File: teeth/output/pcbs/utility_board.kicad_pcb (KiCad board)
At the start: 2 copper layers, 100 x 100 mm, 1 part

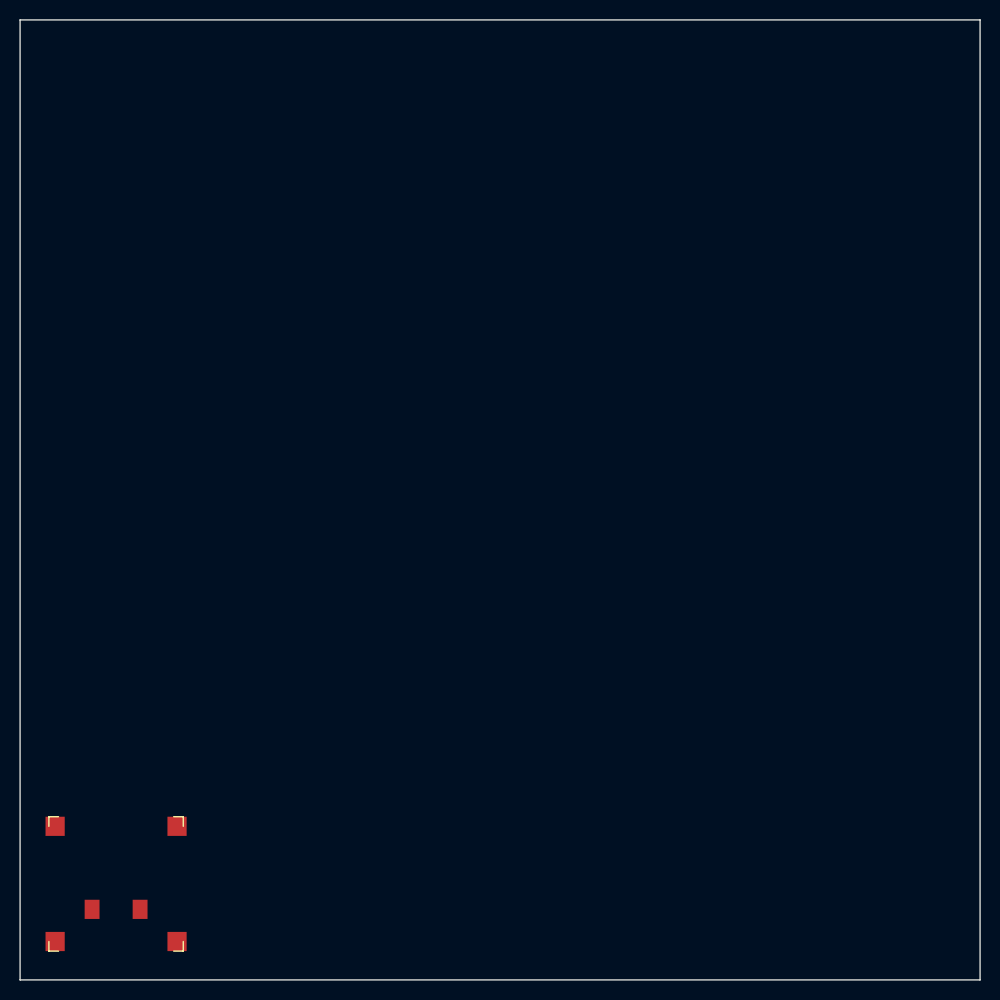
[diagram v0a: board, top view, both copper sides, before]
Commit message: Add xiao cutout footprint to utility board.
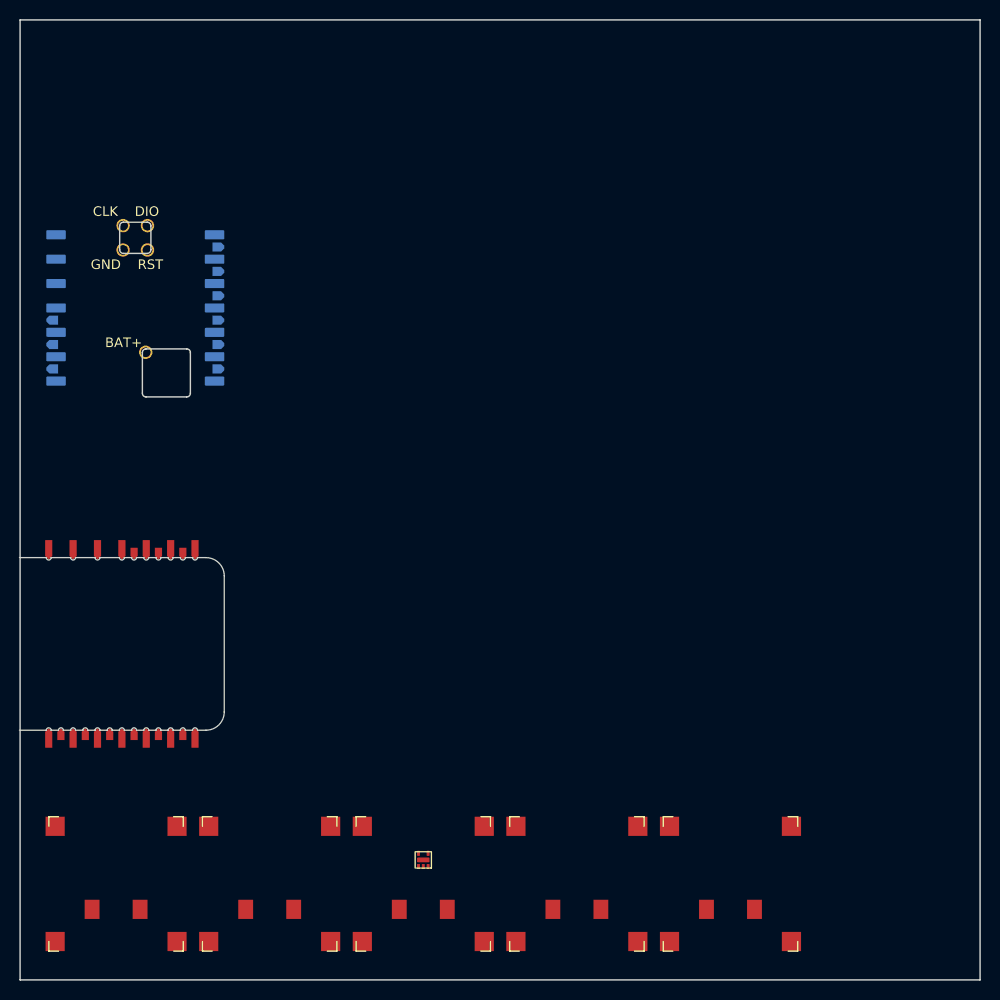
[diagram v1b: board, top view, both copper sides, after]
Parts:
- added D1: , D_MMBD4148PLM, F.Cu at (142.0, 187.5)
- added J1: , xiao_plus_cutout, F.Cu at (110.6, 165.0)
- added S2: , PG1316S, F.Cu at (126.0, 190.0)
- added S3: , PG1316S, F.Cu at (142.0, 190.0)
- added S4: , PG1316S, F.Cu at (158.0, 190.0)
- added S5: , PG1316S, F.Cu at (174.0, 190.0)
- added XX1: , xiao_plus_smd_prod, B.Cu at (112.0, 130.0)
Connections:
- S1 pad 1: firstcol_firstrow -> pinky_home

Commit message: More work on utility board, complex xiao slot complete. Fixed email address.
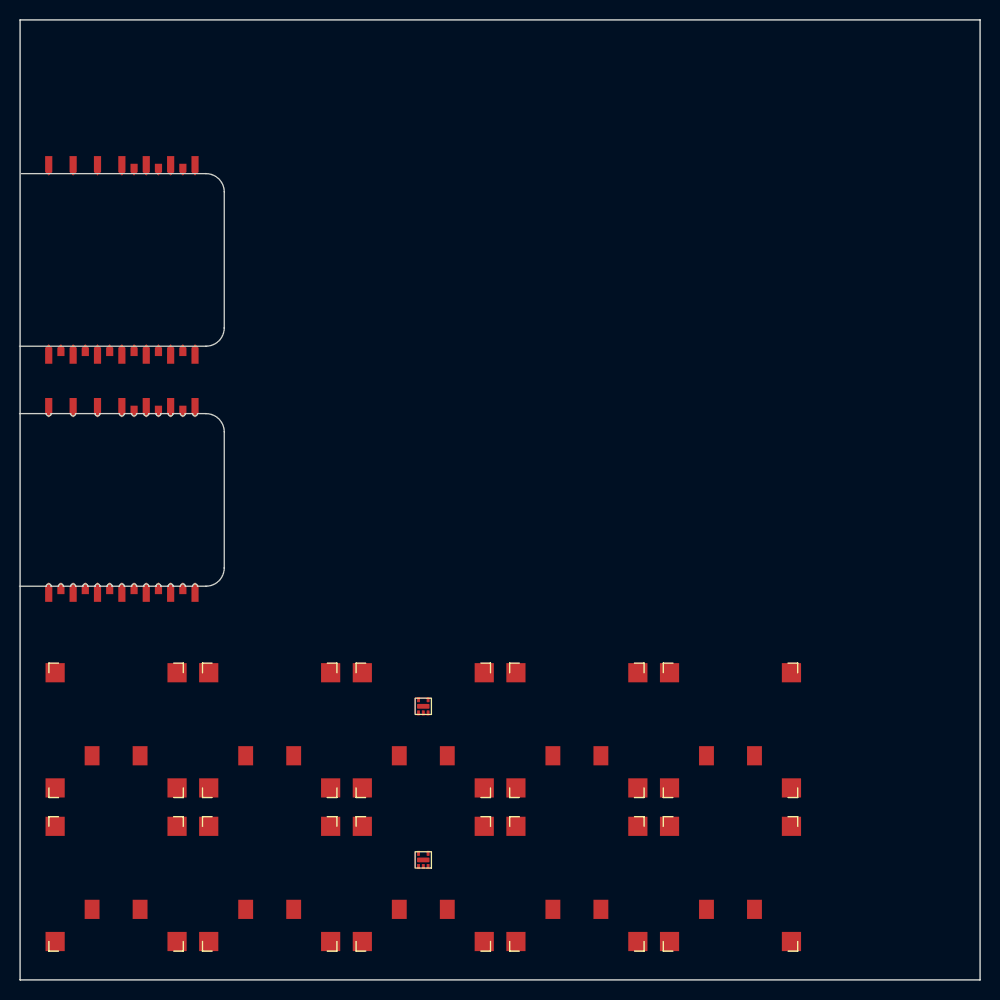
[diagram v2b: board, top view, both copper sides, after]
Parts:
- removed XX1: , xiao_plus_smd_prod
- added D2: , D_MMBD4148PLM, F.Cu at (142.0, 171.5)
- added J2: , xiao_plus_cutout, F.Cu at (110.6, 125.0)
- added S10: , PG1316S, F.Cu at (174.0, 174.0)
- added S6: , PG1316S, F.Cu at (142.0, 174.0)
- added S7: , PG1316S, F.Cu at (158.0, 190.0)
- added S8: , PG1316S, F.Cu at (158.0, 174.0)
- added S9: , PG1316S, F.Cu at (174.0, 190.0)
- moved S4 35.8 mm to (126.0, 174.0)
- moved S5 32.0 mm to (142.0, 190.0)
- moved S2 22.6 mm to (110.0, 174.0)
- moved S3 16.0 mm to (126.0, 190.0)
- moved J1 15.0 mm to (110.6, 150.0)
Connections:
- D1 pad 6: D8 -> P0.03
- S1 pad 2: D5 -> P0.02
- S2 pad 1: ring_home -> pinky_top
- S2 pad 2: D4 -> P0.02
- S3 pad 1: middle_home -> ring_home
- S3 pad 2: D3 -> P0.15
- S4 pad 1: index_home -> ring_top
- S4 pad 2: D2 -> P0.15
- S5 pad 1: inner_home -> middle_home
- S5 pad 2: D1 -> P1.13

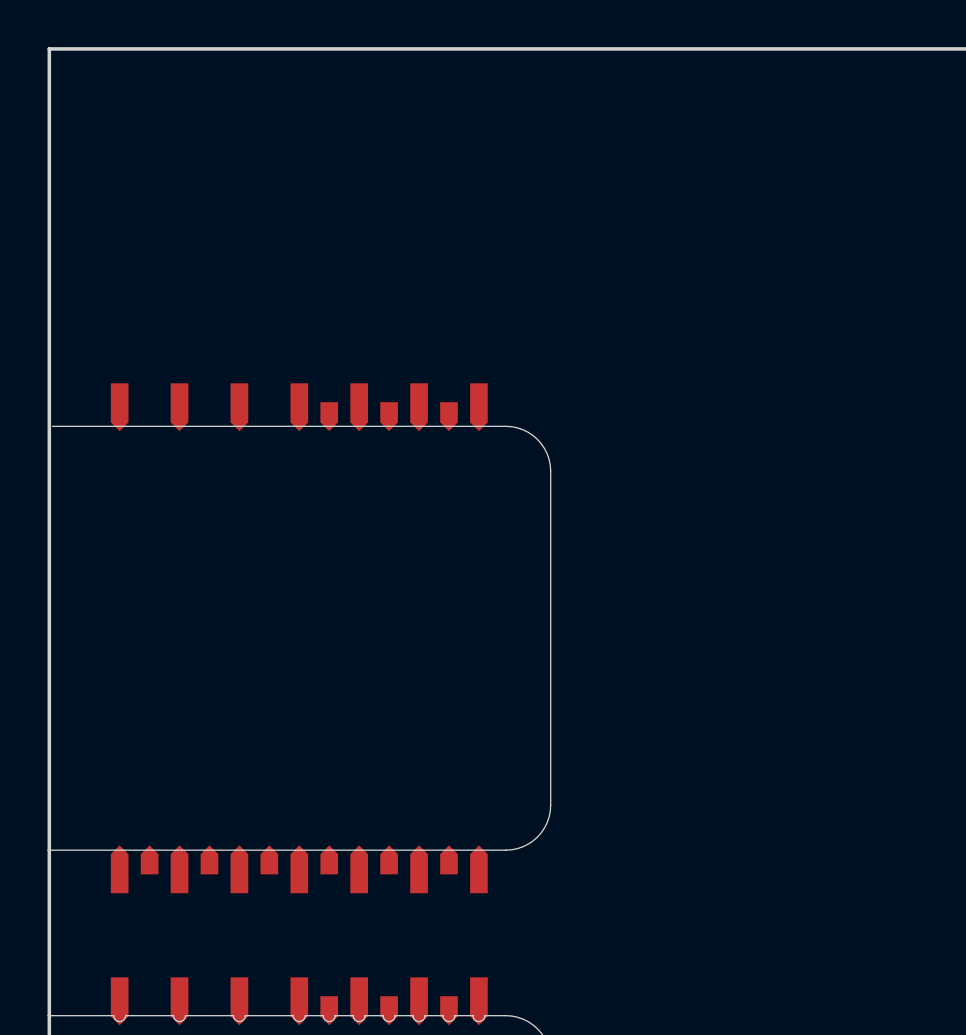
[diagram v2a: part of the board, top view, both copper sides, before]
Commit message: Add through-hole array for xiao breakouts, clean up simple cutout, fix nets.
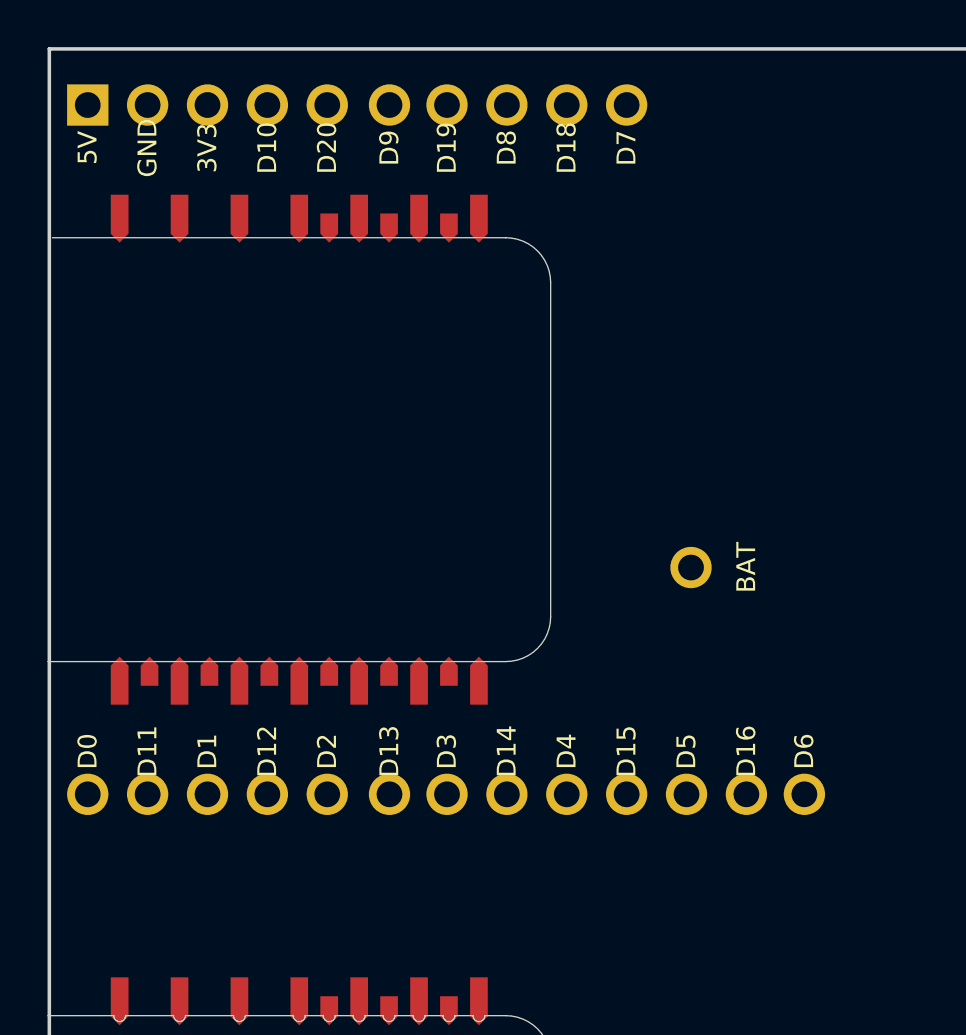
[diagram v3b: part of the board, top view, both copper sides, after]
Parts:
- added MCU1: , XIAO_Breakout_Holes, F.Cu at (110.6, 117.0)
- moved J2 8.00 mm to (110.6, 117.0)
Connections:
- J2 pad 1: P0.02 -> D0_a
- J2 pad 10: P1.14 -> D9_a
- J2 pad 11: P1.15 -> D10_a
- J2 pad 12: 3V3 -> 3V3_a
- J2 pad 13: GND -> GND_a
- J2 pad 14: 5V -> 5V_a
- J2 pad 15: P0.15 -> D11_a
- J2 pad 16: P0.19 -> D12_a
- J2 pad 17: P1.01 -> D13_a
- J2 pad 18: P0.09 -> D14_a
- J2 pad 19: P0.10 -> D15_a
- J2 pad 2: P0.03 -> D1_a
- J2 pad 20: P0.31 -> D16_a
- J2 pad 21: P1.03 -> D17_a
- J2 pad 22: P1.05 -> D18_a
- J2 pad 23: P1.07 -> D19_a
- J2 pad 3: P0.28 -> D2_a
- J2 pad 4: P0.29 -> D3_a
- J2 pad 5: P0.04 -> D4_a
- J2 pad 6: P0.05 -> D5_a
- J2 pad 7: P1.11 -> D6_a
- J2 pad 8: P1.12 -> D7_a
- J2 pad 9: P1.13 -> D8_a

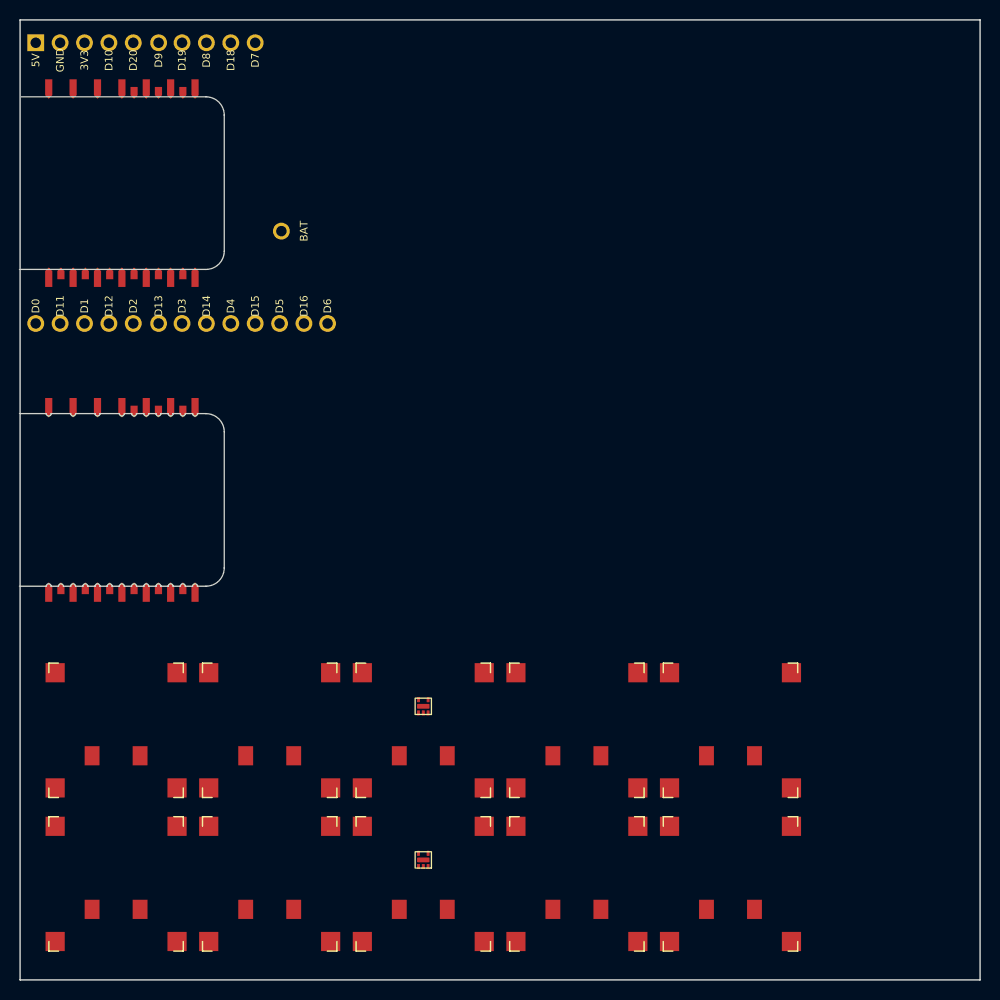
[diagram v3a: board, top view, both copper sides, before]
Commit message: Add wire holes on xiao slots, work on layout.
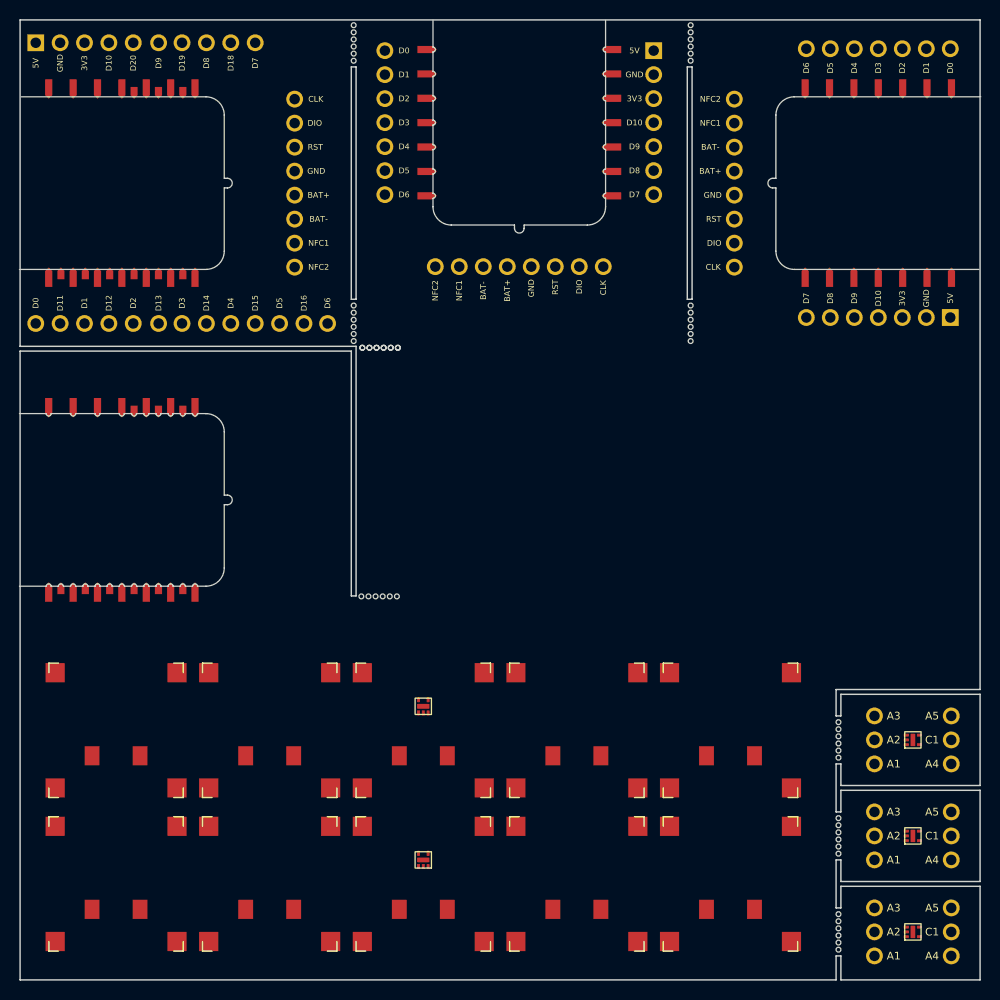
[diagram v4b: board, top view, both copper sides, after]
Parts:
- added D3: , D_MMBD4148PLM, F.Cu at (193.0, 175.0)
- added D4: , D_MMBD4148PLM, F.Cu at (142.0, 187.5)
- added D5: , D_MMBD4148PLM, F.Cu at (142.0, 171.5)
- added J3: , xiao_plus_cutout, F.Cu at (189.4, 117.0)
- added J4: , xiao_plus_cutout, F.Cu at (152.0, 110.7)
- added MCU2: , XIAO_Breakout_Holes, F.Cu at (189.4, 117.0)
- added MCU3: , XIAO_Breakout_Holes, F.Cu at (152.0, 110.7)
- added XX1: mousebites 2mm, mousebites_25mm, F.Cu at (134.8, 102.4)
- added XX10: mousebites 2mm, mousebites_25mm, F.Cu at (185.3, 195.0)
- added XX11: , 5diode_Breakout_Holes, F.Cu at (193.0, 195.0)
- added XX12: , 5diode_Breakout_Holes, F.Cu at (193.0, 185.0)
- added XX13: , 5diode_Breakout_Holes, F.Cu at (193.0, 175.0)
- added XX2: mousebites 2mm, mousebites_25mm, F.Cu at (134.8, 131.6)
- added XX3: mousebites 2mm, mousebites_25mm, F.Cu at (137.4, 160.0)
- added XX4: mousebites 2mm, mousebites_25mm, F.Cu at (169.9, 102.4)
- added XX5: mousebites 2mm, mousebites_25mm, F.Cu at (169.9, 131.6)
- added XX6, XX7: mousebites 2mm, mousebites_25mm, F.Cu at (137.5, 134.1)
- added XX8: mousebites 2mm, mousebites_25mm, F.Cu at (185.3, 175.0)
- added XX9: mousebites 2mm, mousebites_25mm, F.Cu at (185.3, 185.0)
- moved D2 52.8 mm to (193.0, 185.0), turned to 90 degrees
- moved D1 51.5 mm to (193.0, 195.0), turned to 90 degrees
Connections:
- D1 pad 1: index_home -> 1A1
- D1 pad 2: middle_home -> 1A2
- D1 pad 3: ring_home -> 1A3
- D1 pad 4: inner_home -> 1A4
- D1 pad 5: pinky_home -> 1A5
- D1 pad 6: P0.03 -> 1C1
- D2 pad 1: index_top -> 2A1
- D2 pad 2: middle_top -> 2A2
- D2 pad 3: ring_top -> 2A3
- D2 pad 4: inner_top -> 2A4
- D2 pad 5: pinky_top -> 2A5
- D2 pad 6: P1.03 -> 2C1
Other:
- outline, holes or cut-outs redrawn
